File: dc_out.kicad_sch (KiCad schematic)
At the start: 0 parts

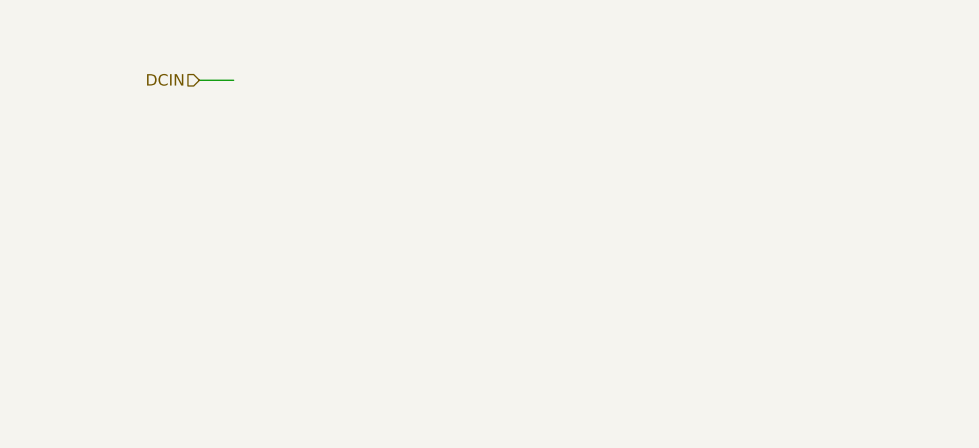
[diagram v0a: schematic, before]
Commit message: Add individually switchable outputs
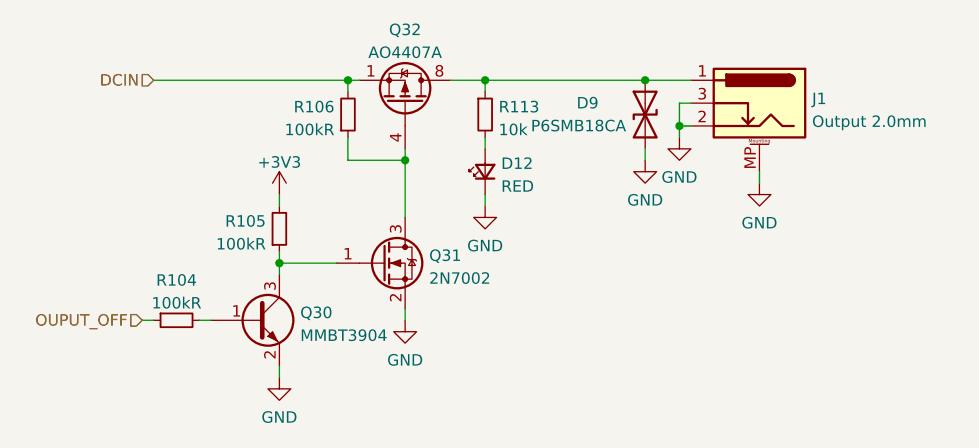
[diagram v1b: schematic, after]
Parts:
- added D12: RED, LED_Indicator:LED_Indicator_RED_MHK1373CRBDT, symbol Device:LED_Small
- added D9: P6SMB18CA, Diode_SMD:D_SMB, symbol Device:D_TVS
- added J1: Output 2.0mm, Connector_BarrelJack_LCSC:BarrelJack_2.0mm_DC-044B, symbol Connector:Barrel_Jack_Switch_MountingPin
- added Q30: MMBT3904, Package_TO_SOT_SMD:SOT-23, symbol Transistor_BJT:MMBT3904
- added Q31: 2N7002, Package_TO_SOT_SMD:SOT-23, symbol Transistor_FET:2N7002
- added Q32: AO4407A, Package_SO:SOIC-8_3.9x4.9mm_P1.27mm, symbol Transistor_FET:FDS9435A
- added R104, R105, R106: 100kR, Resistor_SMD:R_0402_1005Metric, symbol Device:R_Small
- added R113: 10k, Resistor_SMD:R_0402_1005Metric, symbol Device:R_Small
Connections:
- net DCIN: now also Q32.1 (S), Q32.2 (S), Q32.3 (S), R106.2
- new net: Q30.3 (C), Q31.1 (G), R105.1
- new net: Q31.3 (D), Q32.4 (G), R106.1
- new net: D9.1 (A1), J1.1, Q32.5 (D), Q32.6 (D), Q32.7 (D), Q32.8 (D), R113.1
- new net: D12.2 (A), R113.2
- new net: Q30.1 (B), R104.2
- new net +3V3: R105.2
- new net GND: D12.1 (K), D9.2 (A2), J1.2, J1.3, J1.MP (MountPin), Q30.2 (E), Q31.2 (S)
- new net OUPUT_OFF: R104.1

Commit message: Fix footprint origins for JLC assembly
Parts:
- Q32: LCSC C16072 -> C35349
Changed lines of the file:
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@@
       (effects (font (size 1.27 1.27) italic) (justify left) hide)
     )
-    (property "Datasheet" "https://datasheet.lcsc.com/szlcsc/Alpha-Omega-Semicon-AOS-AO4407A_C16072.pdf" (id 3) (at 60.96 63.5 90)
+    (property "Datasheet" "https://datasheet.lcsc.com/szlcsc/Alpha-Omega-Semicon-AOS-AO4407A_C35349.pdf" (id 3) (at 60.96 63.5 90)
       (effects (font (size 1.27 1.27)) (justify left) hide)
     )
-    (property "LCSC" "C16072" (id 4) (at 60.96 63.5 0)
+    (property "LCSC" "C35349" (id 4) (at 60.96 63.5 0)
       (effects (font (size 1.27 1.27)) hide)
     )

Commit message: Fix incorrect AO447A partnumber
The previous partnumber was pointing to a N-Channel MOSFET.
Use a P-Channel one.
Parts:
- Q32: LCSC C35349 -> C167517
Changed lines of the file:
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@@
       (effects (font (size 1.27 1.27)) (justify left) hide)
     )
-    (property "LCSC" "C35349" (id 4) (at 60.96 63.5 0)
+    (property "LCSC" "C167517" (id 4) (at 60.96 63.5 0)
       (effects (font (size 1.27 1.27)) hide)
     )

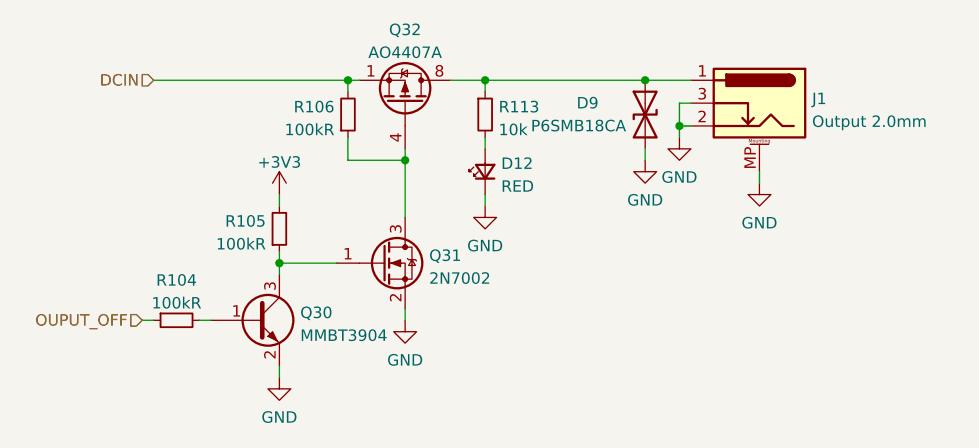
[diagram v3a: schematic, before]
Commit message: Rev 1.0 bugfixes
Changes:
 - Replace DCOK-driven DC passthrough switch with ideal diode
 - Reduce INA219 series filter resistance to 1 ohm
 - Simplify debug USB power gating
 - Fix incorrect USB CC pullups
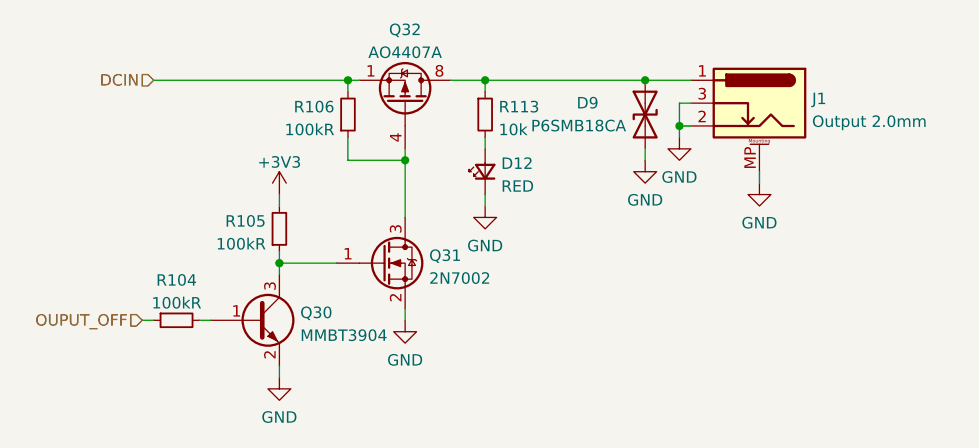
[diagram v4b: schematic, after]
